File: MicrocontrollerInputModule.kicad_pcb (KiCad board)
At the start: 2 copper layers, 33.8 x 42.6 mm, 50 parts, among them J1 Conn_02x04_Odd_Even, J2 IPEX 20655-045E-01, U1 W25Q16JVUXIQ, U2 RP2040, U3 MCP23S17_ML, Y1 12.000MHz

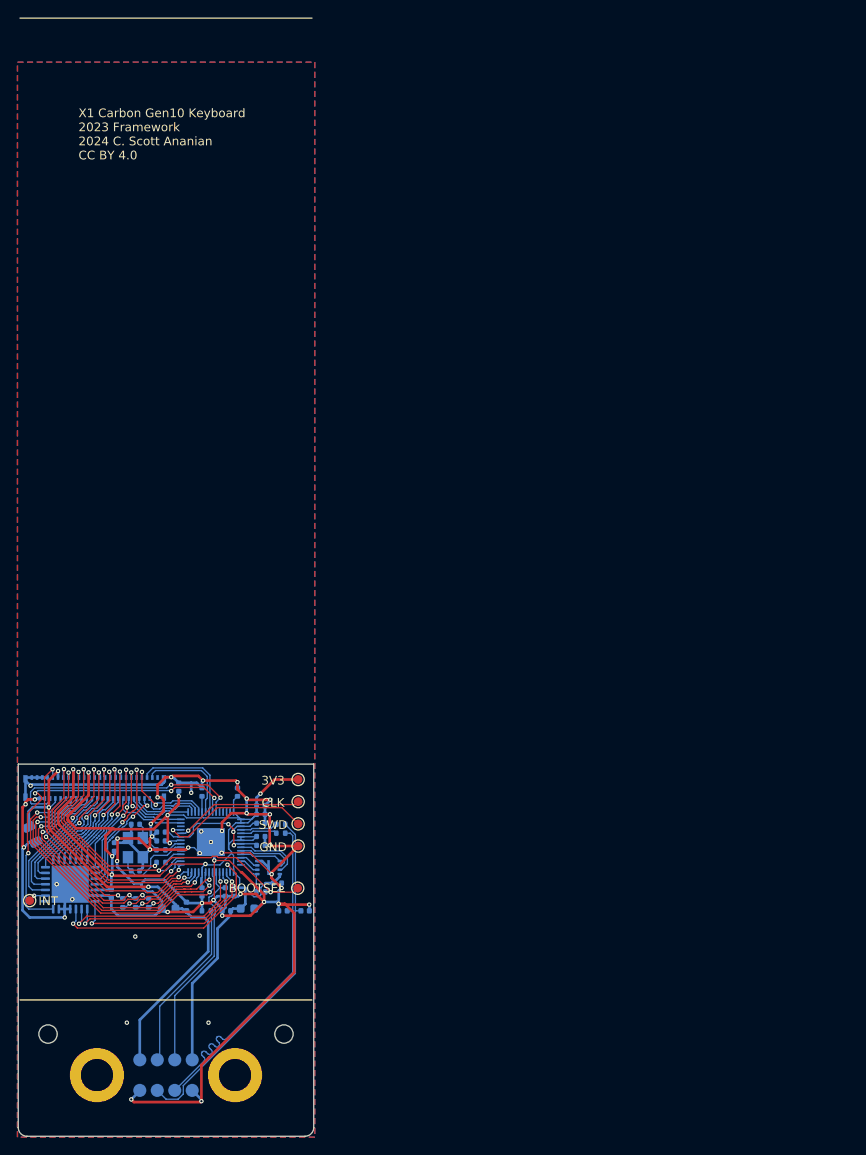
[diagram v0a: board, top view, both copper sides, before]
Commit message: Size test for relocating the FPC connector
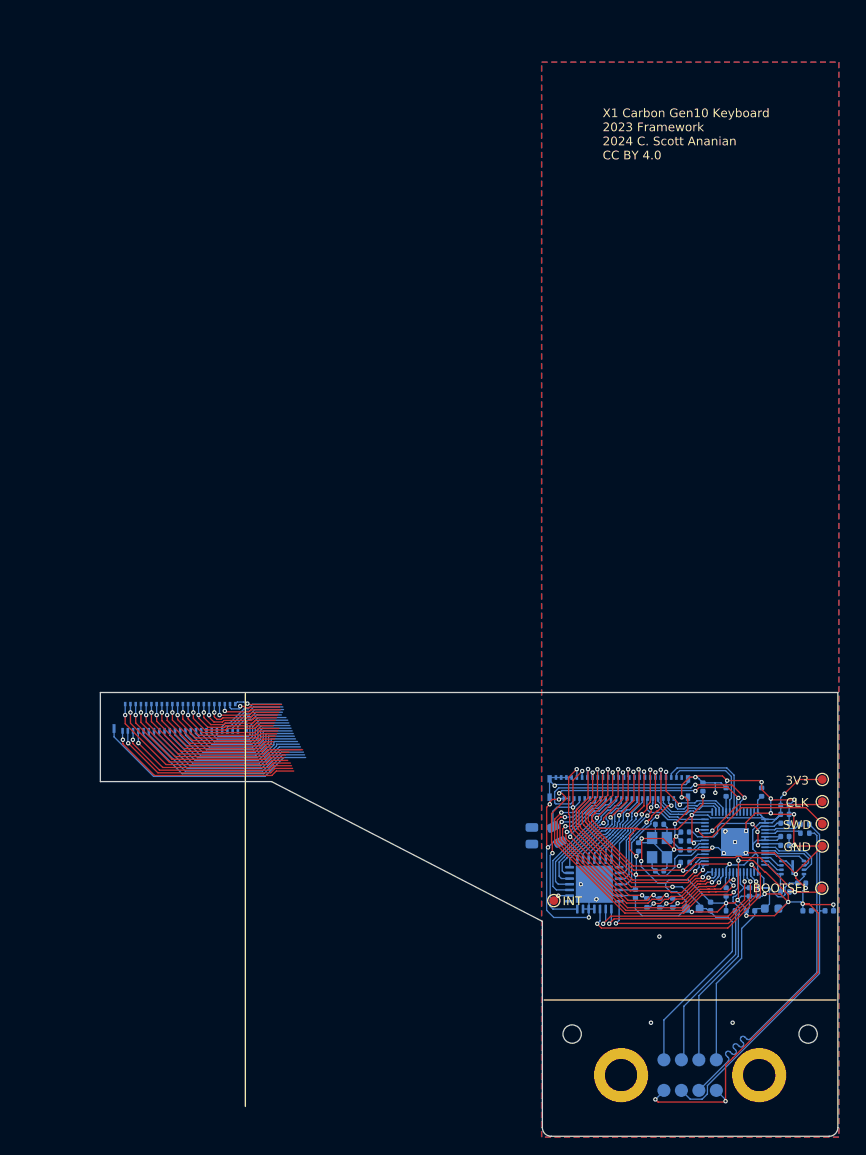
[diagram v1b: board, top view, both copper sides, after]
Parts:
- added C21: 22uF, Capacitor_SMD:C_0805_2012Metric, B.Cu at (108.8, 146.6)
- added J3: IPEX 20655-045E-01, 20655-045E-01:0.3K-HX-45PWB, B.Cu at (68.5, 133.4)
- C19: value 47uF -> 22uF
- moved C12 60.0 mm to (134.7, 153.0)
- moved C13 60.0 mm to (135.1, 141.6)
- moved C8 60.0 mm to (136.2, 154.9)
- moved U2 60.0 mm to (132.1, 147.3)
- moved H1 60.0 mm to (119.0, 174.0)
- moved R8 60.0 mm to (123.4, 154.3)
- moved TP6 60.0 mm to (111.3, 154.0)
- moved C17 60.0 mm to (126.3, 147.2)
- moved C18 60.0 mm to (121.0, 147.9)
- moved C2 60.0 mm to (123.4, 150.6)
- moved C20 60.0 mm to (128.4, 141.0)
- moved C3 60.0 mm to (123.4, 145.3)
- moved C4 60.0 mm to (126.3, 146.2)
- moved C5 60.0 mm to (127.2, 154.9)
- moved D1 60.0 mm to (133.8, 155.2)
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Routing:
- net Net-(J3-LOCK-PadLOCK1): track 0.00 -> 30.8 mm
- net unconnected-(J3-Pad44): track 0.00 -> 23.0 mm, vias 0 -> 1
- net unconnected-(J3-Pad45): track 0.00 -> 22.8 mm, vias 0 -> 1
- net unconnected-(J3-Pad43): track 0.00 -> 21.9 mm, vias 0 -> 1
- net unconnected-(J3-Pad42): track 0.00 -> 21.8 mm, vias 0 -> 1
- net unconnected-(J3-Pad36): track 0.00 -> 21.7 mm, vias 0 -> 1
- net unconnected-(J3-Pad37): track 0.00 -> 21.6 mm
- net unconnected-(J3-Pad40): track 0.00 -> 21.2 mm, vias 0 -> 1
- net unconnected-(J3-Pad41): track 0.00 -> 21.1 mm, vias 0 -> 1
- net unconnected-(J3-Pad38): track 0.00 -> 20.9 mm, vias 0 -> 1
- net unconnected-(J3-Pad35): track 0.00 -> 20.8 mm
- net unconnected-(J3-Pad39): track 0.00 -> 20.2 mm, vias 0 -> 1
- net unconnected-(J3-Pad33): track 0.00 -> 19.9 mm
- net unconnected-(J3-Pad31): track 0.00 -> 19.0 mm
- net unconnected-(J3-Pad29): track 0.00 -> 18.2 mm
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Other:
- board size 33.8 x 42.6 mm -> 84.4 x 50.8 mm

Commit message: Update to use new FPC connector and position, fix sense resistor, etc
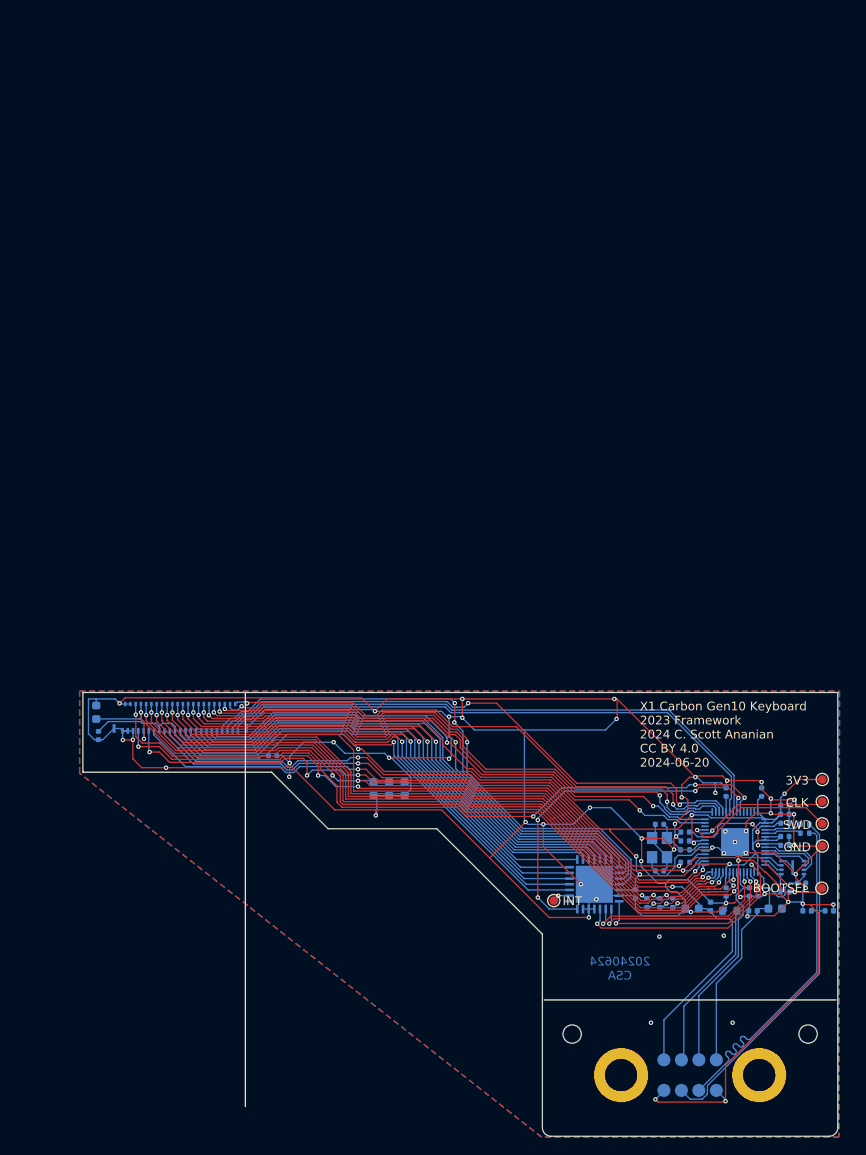
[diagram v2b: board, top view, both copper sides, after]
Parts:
- removed the J2 at (118.8, 141.1)
- added C22: 10uF, Capacitor_SMD:C_0603_1608Metric, B.Cu at (92.5, 141.2)
- added C23: 10uF, Capacitor_SMD:C_0603_1608Metric, B.Cu at (94.2, 141.2)
- C19, C21: value 22uF -> 10uF; footprint Capacitor_SMD:C_0805_2012Metric -> Capacitor_SMD:C_0603_1608Metric
- J2: renamed from J3; value IPEX 20655-045E-01 -> 0.3K-HX-45PWB
- R2: value 180k -> 330k; footprint Resistor_SMD:R_0402_1005Metric -> Resistor_SMD:R_0603_1608Metric
- moved C18 63.1 mm to (59.2, 135.1), turned to 90 degrees
- moved C21 51.8 mm to (58.9, 132.5), turned to -90 degrees
- moved C20 49.4 mm to (79.1, 137.4), turned to 180 degrees
- moved C19 21.6 mm to (90.7, 141.2), turned to 90 degrees
- moved C8 0.41 mm to (136.7, 154.9)
- moved D1 0.28 mm to (134.1, 155.2)
- moved C5 0.10 mm to (127.1, 154.9)
- moved R2 0.10 mm to (131.4, 155.2)
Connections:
- J2 pad 1: unconnected-(J3-Pad1) -> /SENSE3
- J2 pad 10: unconnected-(J3-Pad10) -> /DRV4
- J2 pad 11: unconnected-(J3-Pad11) -> /DRV2
- J2 pad 12: unconnected-(J3-Pad12) -> /SENSE5
- J2 pad 13: unconnected-(J3-Pad13) -> /DRV1
- J2 pad 14: unconnected-(J3-Pad14) -> /DRV3
- J2 pad 15: unconnected-(J3-Pad15) -> /DRV6
- J2 pad 16: unconnected-(J3-Pad16) -> /DRV7
- J2 pad 17: unconnected-(J3-Pad17) -> /DRV5
- J2 pad 18: unconnected-(J3-Pad18) -> /DRV15
- J2 pad 19: unconnected-(J3-Pad19) -> /DRV13
- J2 pad 2: unconnected-(J3-Pad2) -> /SENSE7
- J2 pad 20: unconnected-(J3-Pad20) -> /DRV9
- J2 pad 21: unconnected-(J3-Pad21) -> /DRV12
- J2 pad 22: unconnected-(J3-Pad22) -> /DRV10
- J2 pad 23: unconnected-(J3-Pad23) -> /DRV8
- J2 pad 24: unconnected-(J3-Pad24) -> /DRV11
- J2 pad 25: unconnected-(J3-Pad25) -> +3V3
- J2 pad 26: unconnected-(J3-Pad26) -> /~{LED_FNLOCK_R}
- J2 pad 27: unconnected-(J3-Pad27) -> /~{LED_MUTE_R}
- J2 pad 28: unconnected-(J3-Pad28) -> /~{LED_MICMUTE_R}
- J2 pad 29: unconnected-(J3-Pad29) -> /~{HOTKEY}
- J2 pad 3: unconnected-(J3-Pad3) -> /SENSE6
- J2 pad 30: unconnected-(J3-Pad30) -> /~{LED_CAPSLOCK_R}
- J2 pad 31: unconnected-(J3-Pad31) -> +3V3
- J2 pad 32: unconnected-(J3-Pad32) -> /TP4DATA
- J2 pad 33: unconnected-(J3-Pad33) -> /TP4RESET
- J2 pad 34: unconnected-(J3-Pad34) -> /TP4CLK
- J2 pad 35: unconnected-(J3-Pad35) -> /~{TP4ACT}
- J2 pad 36: unconnected-(J3-Pad36) -> /~{TP4_FW_WR_EN}
- J2 pad 37: unconnected-(J3-Pad37) -> +5V
- J2 pad 38: unconnected-(J3-Pad38) -> +5V
- J2 pad 39: unconnected-(J3-Pad39) -> /KBD_BL_PWM
- J2 pad 4: unconnected-(J3-Pad4) -> /DRV14
- J2 pad 40: unconnected-(J3-Pad40) -> /~{KBD_BL_DET}
- J2 pad 41: unconnected-(J3-Pad41) -> GND
- J2 pad 42: unconnected-(J3-Pad42) -> GND
- J2 pad 43: unconnected-(J3-Pad43) -> GND
- J2 pad 44: unconnected-(J3-Pad44) -> GND
- J2 pad 45: unconnected-(J3-Pad45) -> GND
- J2 pad 5: unconnected-(J3-Pad5) -> /SENSE4
- J2 pad 6: unconnected-(J3-Pad6) -> /SENSE1
- J2 pad 7: unconnected-(J3-Pad7) -> /DRV0
- J2 pad 8: unconnected-(J3-Pad8) -> /SENSE2
- J2 pad 9: unconnected-(J3-Pad9) -> /SENSE0
- J2 pad LOCK1: Net-(J3-LOCK-PadLOCK1) -> GND
- J2 pad LOCK2: Net-(J3-LOCK-PadLOCK1) -> GND
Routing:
- net GND: track 262.2 -> 495.9 mm, vias 45 -> 60
- net +5V: track 55.5 -> 113.7 mm, vias 3 -> 5
- net /SENSE1: track 7.84 -> 64.8 mm, vias 0 -> 2
- net /SENSE2: track 7.42 -> 64.2 mm, vias 0 -> 2
- net /SENSE7: track 7.17 -> 63.0 mm, vias 0 -> 2
- net /SENSE5: track 8.55 -> 64.3 mm, vias 0 -> 2
- net /SENSE4: track 11.0 -> 65.5 mm
- net /~{KBD_BL_DET}: track 28.5 -> 82.9 mm, vias 2 -> 4
- net /SENSE3: track 11.3 -> 65.4 mm
- net /SENSE6: track 12.5 -> 66.5 mm
- net /SENSE0: track 10.7 -> 63.1 mm
- net /DRV4: track 10.4 -> 59.6 mm
- net /~{TP4_FW_WR_EN}: track 34.7 -> 83.8 mm
- net /~{LED_FNLOCK_R}: track 18.6 -> 67.6 mm
- net /TP4CLK: track 33.7 -> 82.5 mm
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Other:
- board size 84.4 x 50.8 mm -> 86.4 x 50.8 mm
- board text added: "20240624 CSA"
- board text added: "X1 Carbon Gen10 Keyboard 2023 Framework 2024 C. Scott Ananian CC BY 4.0 2024-06-20"
- board text removed: "X1 Carbon Gen10 Keyboard 2023 Framework 2024 C. Scott Ananian CC BY 4.0"

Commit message: Second version sent to JLCPCB
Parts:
- added H5: Tooling Hole, 20655-045E-01:JLCPCB Tooling Hole, F.Cu at (142.4, 131.7)
- added H6: Tooling Hole, 20655-045E-01:JLCPCB Tooling Hole, F.Cu at (111.5, 179.7)
- added H7: Tooling Hole, 20655-045E-01:JLCPCB Tooling Hole, F.Cu at (142.4, 179.6)
- added H8: Tooling Hole, 20655-045E-01:JLCPCB Tooling Hole, F.Cu at (58.7, 137.9)
- moved D4 0.35 mm to (142.5, 155.2)
- moved C18 0.13 mm to (59.1, 135.1)
- moved C21 0.13 mm to (58.8, 132.5)
- moved D3 0.10 mm to (140.2, 155.2)
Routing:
- net GND: track 495.9 -> 504.2 mm
- net Net-(U3-INTA): track 2.07 -> 4.32 mm
- net +3V3: track 185.2 -> 186.0 mm
- net /~{HOTKEY}: track 89.2 -> 89.8 mm
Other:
- board text added: "1"
- board text added: "JLCJLCJLCJLC"
